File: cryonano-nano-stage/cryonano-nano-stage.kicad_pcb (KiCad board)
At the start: 4 copper layers, 100 x 75 mm, 173 parts, among them J1 24VDC IN, J2 JST-B2B-XH-AM, J3 JST-B2B-XH-AM, J5 JST-B3B-XH-AM, J6 RJ45_Hanrun_HR911105A_Horizon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, J8 Conn_ST_STDC14, J9 USB4930-00-A, Q1 PMV100EPAR, SW1 BOOT, SW2 RESET, U1 AD7124-8BCPZ-RL7, U10 LAN8742A, U2 NUP4106DR2G, U3 1ED3141MU12FXUMA1, U4 AP7363-33D-13, U5 ECMF02-2AMX6, U6 LP5907MFX-3.3_NOPB, U7 STM32H753ZITx, Y3 25.0MHz

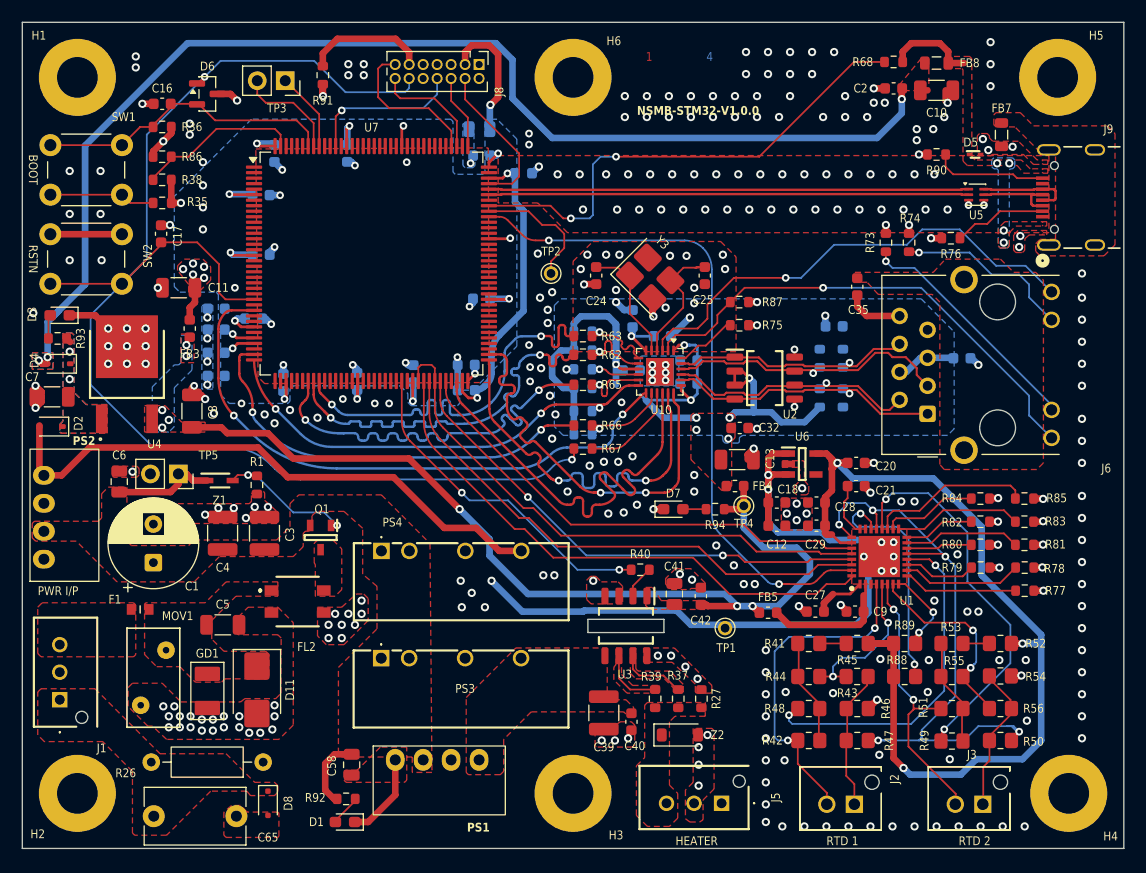
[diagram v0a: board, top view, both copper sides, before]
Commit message: bom adjusted
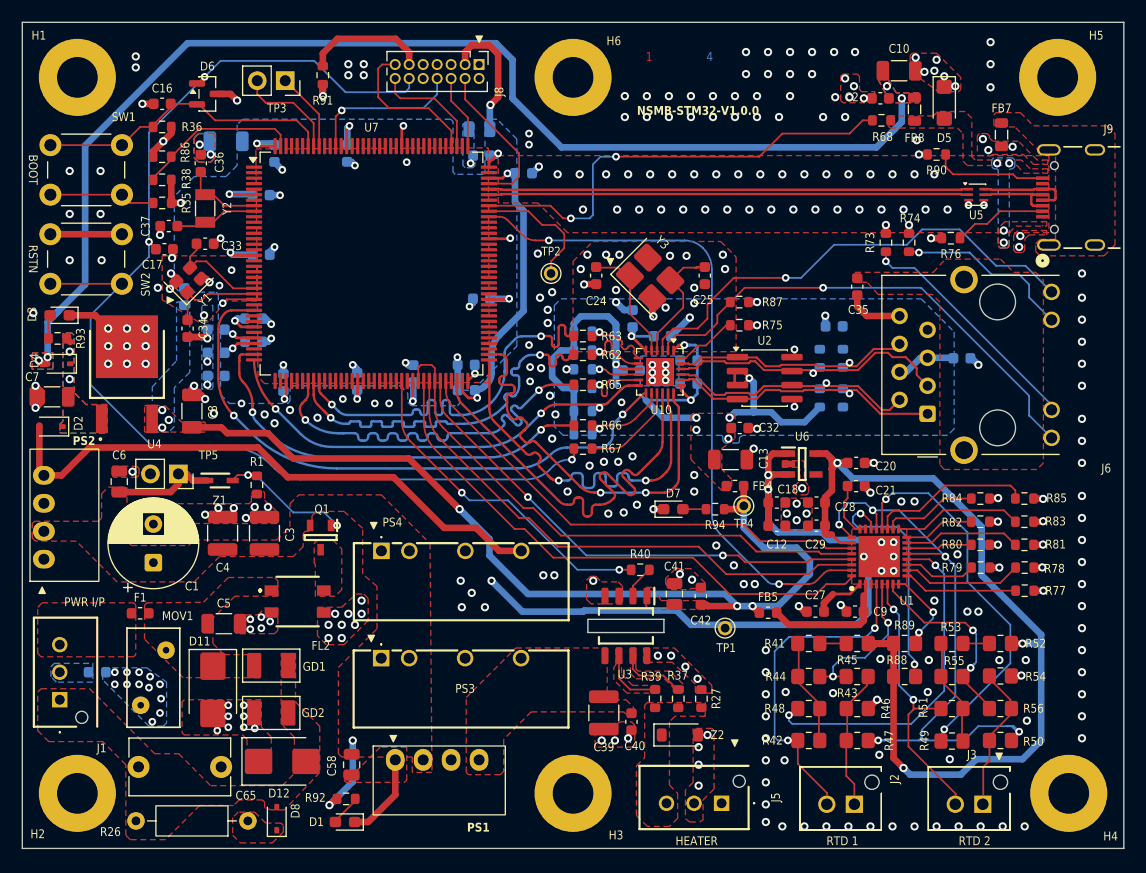
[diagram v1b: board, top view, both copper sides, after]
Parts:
- added C33: 33pF, Capacitor_SMD:C_0603_1608Metric, F.Cu at (56.6, 85.1)
- added C34: 33pF, Capacitor_SMD:C_0603_1608Metric, F.Cu at (55.0, 92.8)
- added C36: 8p, Capacitor_SMD:C_0603_1608Metric, F.Cu at (56.2, 77.8)
- added C37: 8p, Capacitor_SMD:C_0603_1608Metric, F.Cu at (53.3, 83.5)
- added D12: SMBJ30CA, Diode_SMD:D_SMB, F.Cu at (63.6, 132.1)
- added F2: 0686F5000-01, Fuse:Fuse_0603_1608Metric, B.Cu at (46.8, 124.0)
- added GD2: B32-150-LF, footprints:B32_GDT_YAGEO, F.Cu at (62.6, 127.7)
- added Y1: 12MHz, Crystal:Crystal_SMD_2520-4Pin_2.5x2.0mm, F.Cu at (55.1, 88.4)
- added Y2: 32.768kHz, Crystal:Crystal_SMD_3215-2Pin_3.2x1.5mm, F.Cu at (56.6, 81.9)
- C11, FB3: moved to B.Cu
- D5: value ESD9X5.0ST5G -> SMF5V0A-M3-08; footprint footprints:SODFL1006X40N -> Diode_SMD:D_SMF
- D8: value PESD12VL1BA -> DF2B36FU,H3XHF; footprint Diode_SMD:D_SOD-323F -> Diode_SMD:D_SOD-323
- F1: value FMC16302WBTP -> 0686F5000-01; footprint footprints:FUSC1608X55N -> Fuse:Fuse_0603_1608Metric
- J1: value 24VDC IN -> JST-B3B-XH-AM
- R40: value 22R -> 33R
- TP1, TP4: value +5V0_1 -> 1x01, 2.54
- TP2: value TEST POINT -> 1x01, 2.54
- TP3, TP5: value 1x02 2.54mm -> 1x02, 2.54
- U2: value NUP4106DR2G -> SRDA3.3-4BTG; footprint footprints:SOIC127P600X175-8N -> Package_SO:SOIC-8_3.9x4.9mm_P1.27mm
- moved C11 14.0 mm to (58.5, 75.8)
- moved GD1 6.24 mm to (62.6, 123.4), turned to 0 degrees
- moved R26 5.51 mm to (60.5, 137.5)
- moved D5 5.47 mm to (123.7, 72.3), turned to -90 degrees
- moved R68 5.41 mm to (118.0, 73.9)
- moved C65 4.68 mm to (58.0, 132.6)
- moved FB8 4.65 mm to (121.0, 72.9), turned to 90 degrees
- moved C54 4.53 mm to (61.0, 94.0), turned to 0 degrees
- moved D11 4.00 mm to (57.3, 125.6)
- moved C10 3.84 mm to (119.6, 69.4)
- moved FB3 2.94 mm to (54.7, 89.9)
- moved D8 1.61 mm to (63.1, 137.3), turned to 90 degrees
- moved C2 1.50 mm to (117.9, 71.9)
- moved C17 1.43 mm to (52.9, 85.6), turned to 0 degrees
- moved C13 0.60 mm to (104.3, 104.7)
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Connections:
- net Net-(C5-Pad1) renamed /Block Diagram/Power/IN_HIGH
- C5 pad 2: /Block Diagram/Power/0V0IN -> /Block Diagram/Power/IN_LOW
- D11 pad 2: /Block Diagram/Power/0V0IN -> /Block Diagram/Power/IN_LOW
- D5 pad 1: /Block Diagram/Communication/USB_VBUS -> GND
- D5 pad 2: GND -> /Block Diagram/Communication/USB_VBUS
- D8 pad 1: Earth -> /Block Diagram/M24V0
- D8 pad 2: /Block Diagram/M24V0 -> Earth
- FL2 pad 2: /Block Diagram/Power/0V0IN -> /Block Diagram/Power/IN_LOW
- GD1 pad 2: /Block Diagram/Power/0V0IN -> Earth
- MOV1 pad 2: /Block Diagram/Power/0V0IN -> /Block Diagram/Power/IN_LOW
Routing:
- net /Block Diagram/Controller/MCU GPIO/RCC_OSC_IN: track 0.00 -> 9.51 mm
- net /Block Diagram/Controller/MCU GPIO/RCC_OSC_OUT: track 0.00 -> 9.06 mm
- net /Block Diagram/Communication/USB_VBUS: track 8.18 -> 0.00 mm
- net /Block Diagram/Controller/MCU GPIO/RCC_OSC32_OUT: track 0.00 -> 6.28 mm
- net /Block Diagram/Controller/MCU GPIO/RCC_OSC32_IN: track 0.00 -> 5.78 mm
- net Net-(U7A-PA9): track 45.0 -> 41.7 mm
- net /Block Diagram/Controller/VDD: track 61.5 -> 58.4 mm, vias 22 -> 17
- net /Block Diagram/Controller/NRST: track 126.8 -> 124.4 mm, vias 2 -> 4
- net GND: track 74.0 -> 75.8 mm, vias 306 -> 312
- net /Block Diagram/+24V0: track 16.0 -> 17.2 mm, vias 0 -> 2
- net V_BUS: track 109.7 -> 109.3 mm, vias 3 -> 4
- net /Block Diagram/Power/IN_LOW: vias 0 -> 25
- net /Block Diagram/Power/0V0IN: vias 21 -> 0
- net /Block Diagram/+3V3: vias 8 -> 6
- added copper zone on B.Cu, net /Block Diagram/Power/0V0IN
- added copper zone on B.Cu, net /Block Diagram/Power/IN_LOW
- added copper zone on F.Cu, net /Block Diagram/Power/IN_LOW
- added copper zone on In1.Cu, net /Block Diagram/Power/IN_LOW
- removed copper zone on F.Cu, net /Block Diagram/Controller/VDD
- removed copper zone on F.Cu, net /Block Diagram/Power/0V0IN
- removed copper zone on In1.Cu, net /Block Diagram/Power/0V0IN

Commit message: drc ok, review schematic
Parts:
- added C60: 100n, Capacitor_SMD:C_0603_1608Metric, F.Cu at (120.2, 121.4)
- added C61: 100n, Capacitor_SMD:C_0603_1608Metric, F.Cu at (100.9, 125.9)
- added FB6: MH1608, Inductor_SMD:L_0603_1608Metric, F.Cu at (98.9, 126.6)
- added R28: 133k, Resistor_SMD:R_0603_1608Metric, F.Cu at (97.8, 123.9)
- added R95: 0R, Resistor_SMD:R_0805_2012Metric_Pad1.20x1.40mm_HandSolder, F.Cu at (120.2, 130.2)
- added R97: 33k, Resistor_SMD:R_0603_1608Metric, F.Cu at (97.8, 122.0)
- added R98: 33k, Resistor_SMD:R_0603_1608Metric, F.Cu at (100.9, 122.5)
- added U8: 1EDN7550BXTSA1, footprints:SOT95P280X145-6N, F.Cu at (104.2, 125.1)
- C39: footprint Capacitor_SMD:C_1210_3225Metric -> Capacitor_SMD:C_0805_2012Metric
- R40: value 33R -> 825R
- U3: value 1ED3141MU12FXUMA1 -> TLP2735(TP,E(O; footprint footprints:SOIC127P600X175-8N -> footprints:SO-6L_10x3.84mm_P1.27mm
- moved R39 8.93 mm to (105.9, 129.3)
- moved R89 5.91 mm to (120.1, 127.3)
- moved R37 5.31 mm to (104.0, 129.3)
- moved R53 4.40 mm to (128.8, 121.4), turned to 0 degrees
- moved R52 4.40 mm to (124.4, 121.4), turned to 0 degrees
- moved R27 2.93 mm to (102.1, 129.3), turned to -90 degrees
- moved C39 2.65 mm to (94.1, 130.0), turned to 180 degrees
- moved U3 2.59 mm to (93.6, 122.1)
- moved C40 2.55 mm to (97.0, 126.6)
- moved TP1 1.99 mm to (105.7, 119.4)
- moved R40 1.61 mm to (94.5, 114.9)
- moved Z2 1.10 mm to (98.6, 129.7), turned to 180 degrees
- moved J1 1.00 mm to (44.4, 126.5)
- moved FB5 0.51 mm to (108.2, 118.5)
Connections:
- net /Block Diagram/Heater Drive/SW_D renamed /Block Diagram/PSW_D
- C39 pad 2: /Block Diagram/Heater Drive/M15V0 -> /Block Diagram/PSW_S
- C40 pad 2: /Block Diagram/Heater Drive/M15V0 -> /Block Diagram/PSW_S
- J5 pad 2: /Block Diagram/Heater Drive/M15V0 -> /Block Diagram/PSW_G
- J5 pad 3: /Block Diagram/Heater Drive/SW_G -> /Block Diagram/PSW_S
- PS1 pad 3: /Block Diagram/Heater Drive/M15V0 -> /Block Diagram/PSW_S
- PS3 pad 4: /Block Diagram/Heater Drive/M15V0 -> /Block Diagram/PSW_S
- R27 pad 1: /Block Diagram/Heater Drive/SW_G -> /Block Diagram/PSW_S
- R27 pad 2: /Block Diagram/Heater Drive/M15V0 -> /Block Diagram/PSW_G
- R37 pad 1: Net-(U3-OUTL) -> Net-(U8-OUT_SRC)
- R37 pad 2: /Block Diagram/Heater Drive/SW_G -> /Block Diagram/PSW_G
- R39 pad 1: Net-(U3-OUTH) -> Net-(U8-OUT_SNK)
- R39 pad 2: /Block Diagram/Heater Drive/SW_G -> /Block Diagram/PSW_G
- R40 pad 2: Net-(U3-IN+) -> Net-(U3-A)
- R45 pad 1: /Block Diagram/ADC/A+3V3 -> /Block Diagram/Interface/EXCITATION
- R52 pad 1: /Block Diagram/ADC/A+3V3 -> /Block Diagram/Interface/EXCITATION
- R88 pad 1: /Block Diagram/ADC/A+3V3 -> /Block Diagram/Interface/EXCITATION
- R89 pad 1: /Block Diagram/ADC/A+3V3 -> /Block Diagram/Interface/EXCITATION
- U3 pad 1: /Block Diagram/+3V3 -> Net-(U3-A)
- U3 pad 2: Net-(U3-IN+) -> unconnected-(U3-N.C-Pad2)
- U3 pad 4: GND -> /Block Diagram/PSW_S
- U3 pad 5: /Block Diagram/Heater Drive/+15V0 -> Net-(U3-VO)
- U3 pad 6: Net-(U3-OUTH) -> /Block Diagram/Heater Drive/+15V0
- Z2 pad 1: /Block Diagram/Heater Drive/SW_G -> /Block Diagram/PSW_G
- Z2 pad 2: /Block Diagram/Heater Drive/M15V0 -> /Block Diagram/PSW_S
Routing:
- net /Block Diagram/Heater Drive/+15V0: track 0.00 -> 21.6 mm
- net /Block Diagram/Interface/EXCITATION: track 0.00 -> 16.1 mm, vias 0 -> 2
- net /Block Diagram/ADC/A+3V3: track 85.8 -> 71.7 mm, vias 3 -> 2
- net /Block Diagram/PSW_S: track 0.00 -> 9.98 mm, vias 0 -> 10
- net Net-(U3-VO): track 0.00 -> 8.16 mm
- net /Block Diagram/ADC/REFIOUT: track 7.15 -> 14.9 mm
- net Net-(U8-IN-): track 0.00 -> 6.09 mm
- net Net-(U8-IN+): track 0.00 -> 5.98 mm
- net Net-(R49-Pad2): track 8.53 -> 14.2 mm
- net Net-(U3-OUTL): track 5.55 -> 0.00 mm
- net Net-(U3-OUTH): track 5.34 -> 0.00 mm
- net /Block Diagram/+3V3: track 83.2 -> 88.4 mm, vias 6 -> 5
- net Net-(U8-VDD): track 0.00 -> 4.78 mm
- net Net-(U3-IN+): track 2.98 -> 0.00 mm
- net /Block Diagram/ADC/REFVOUT: track 21.7 -> 24.3 mm
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- added copper zone on F.Cu, net /Block Diagram/PSW_G
- added copper zone on In1.Cu, net /Block Diagram/PSW_S
- removed copper zone on F.Cu, net /Block Diagram/Heater Drive/M15V0
- removed copper zone on In1.Cu, net /Block Diagram/Heater Drive/M15V0
- removed copper zone on F.Cu, net /Block Diagram/Heater Drive/SW_G
- removed copper zone on F.Cu, net Net-(U3-OUTH)
- removed copper zone on F.Cu, net Net-(U3-OUTL)
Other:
- outline, holes or cut-outs redrawn
- board text added: "+"
- board text added: "-"
- board text added: "24V DC IN"
- board text added: "ADC"
- board text added: "BRIDGE INTERFACE"
- board text added: "D"
- board text added: "DEBUG"
- board text added: "ETHERNET"
- board text added: "G"
- board text added: "POWER"
- board text added: "PWM"
- board text added: "RESET"
- board text added: "S"
- board text added: "STDC14"
- board text added: "USB"
- board text removed: "PWR I/P"
- board text removed: "RSTN"

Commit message: drc ok. chip level review pending
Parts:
- added C62: 100n, Capacitor_SMD:C_0603_1608Metric, F.Cu at (99.4, 129.9)
- added R96: 6R2, Resistor_SMD:R_0603_1608Metric, F.Cu at (96.0, 129.9)
- moved TP1 8.78 mm to (97.0, 118.2)
- moved C61 3.51 mm to (101.1, 122.4), turned to 180 degrees
- moved FB6 3.11 mm to (101.1, 124.4), turned to 0 degrees
- moved R98 2.44 mm to (102.3, 120.5), turned to 0 degrees
- moved C40 2.31 mm to (97.7, 124.4), turned to 180 degrees
- moved Z2 2.20 mm to (98.6, 127.5)
- moved R97 1.53 mm to (98.1, 120.5)
- moved R28 1.50 mm to (97.7, 122.4)
- moved U8 1.39 mm to (104.9, 123.9)
- moved C39 1.12 mm to (93.1, 129.5), turned to -90 degrees
- moved U3 0.40 mm to (93.6, 121.7)
- moved R27 0.20 mm to (102.1, 129.1)
- moved R37 0.20 mm to (104.0, 129.1)
- moved R39 0.20 mm to (105.9, 129.1)
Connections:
- net /Block Diagram/Controller/ID renamed /Block Diagram/Controller/MCU GPIO/USB_ID
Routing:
- net /Block Diagram/+3V3: track 88.4 -> 94.0 mm
- net /Block Diagram/+5V0: track 115.9 -> 112.4 mm, vias 5 -> 4
- net /Block Diagram/Heater Drive/+15V0: track 21.6 -> 24.6 mm, vias 0 -> 2
- net Net-(U8-IN-): track 6.09 -> 4.26 mm
- net Net-(C62-Pad2): track 0.00 -> 1.80 mm
- net /Block Diagram/Controller/VDD: track 58.4 -> 56.7 mm
- net Net-(U8-OUT_SRC): track 2.21 -> 3.50 mm
- net Net-(U3-VO): track 8.16 -> 9.15 mm
- net /Block Diagram/Controller/MCU Power/VCAP: track 27.0 -> 28.0 mm
- net Net-(U8-OUT_SNK): track 2.44 -> 3.08 mm

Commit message: sch reviewed
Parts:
- added C63: 680p, Capacitor_SMD:C_0603_1608Metric, B.Cu at (104.4, 127.2)
- added D9: SMBJE36CAH, Diode_SMD:D_SMB, B.Cu at (100.4, 131.6)
- added R100: 6R2, Resistor_SMD:R_2010_5025Metric, B.Cu at (102.0, 123.7)
- added R29: 2.7k, Resistor_SMD:R_0805_2012Metric, B.Cu at (80.3, 135.0)
- added R30: 2.7k, Resistor_SMD:R_0805_2012Metric, B.Cu at (45.1, 107.3)
- added R99: 56R, Resistor_SMD:R_2010_5025Metric, B.Cu at (100.0, 127.3)
- C62: value 100n -> 680p
- moved R37 1.90 mm to (105.9, 129.1)
- moved R39 1.90 mm to (104.0, 129.1)
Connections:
- net Net-(TP3-Pin_1) renamed /Block Diagram/Controller/MCU GPIO/SCL
- net Net-(TP3-Pin_2) renamed /Block Diagram/Controller/MCU GPIO/SDA
- R37 pad 1: Net-(U8-OUT_SRC) -> Net-(U8-OUT_SNK)
- R39 pad 1: Net-(U8-OUT_SNK) -> Net-(U8-OUT_SRC)
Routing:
- net /Block Diagram/PSW_S: track 9.84 -> 15.6 mm, vias 10 -> 15
- net GND: track 76.4 -> 79.7 mm
- net /Block Diagram/Power/+5V0: track 52.2 -> 55.5 mm
- net /Block Diagram/Heater Drive/+15V0: track 24.6 -> 25.5 mm, vias 2 -> 0
- net /Block Diagram/+5V0: track 112.4 -> 113.1 mm
- added copper zone on B.Cu, net /Block Diagram/PSW_D
- added copper zone on B.Cu, net /Block Diagram/PSW_S
- added copper zone on F.Cu, net /Block Diagram/PSW_S
- added copper zone on B.Cu, net Net-(C63-Pad1)
- added copper zone on B.Cu, net Net-(C63-Pad2)
